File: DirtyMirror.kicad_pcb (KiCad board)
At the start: 2 copper layers, 53 parts, among them J101 PWR, SW101 SW_SPDT, U101 TL074, U102 TL074, U103 TL072

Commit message: routed & DRC passing
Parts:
- added C109: 4n7, Capacitor_SMD:C_0805_2012Metric, B.Cu at (21.7, 62.6)
- added C111: 2n2, Capacitor_SMD:C_0805_2012Metric, B.Cu at (14.1, 66.5)
- added J102: ScopeGroundLoop, Connector:THT_GND_WIRE, B.Cu at (84.7, 68.4)
- added TP101: In, TestPoint:TestPoint_THTPad_D2.0mm_Drill1.0mm_VAL, B.Cu at (36.4, 88.2)
- added TP102: Out, TestPoint:TestPoint_THTPad_D2.0mm_Drill1.0mm_VAL, B.Cu at (60.7, 86.5)
- added TP103: LT, TestPoint:TestPoint_THTPad_D2.0mm_Drill1.0mm_VAL, B.Cu at (30.9, 80.1)
- added TP104: HT, TestPoint:TestPoint_THTPad_D2.0mm_Drill1.0mm_VAL, B.Cu at (16.1, 82.2)
- added TP105: Bias, TestPoint:TestPoint_THTPad_D2.0mm_Drill1.0mm_VAL, B.Cu at (46.9, 67.2)
- added TP106: LR, TestPoint:TestPoint_THTPad_D2.0mm_Drill1.0mm_VAL, B.Cu at (64.2, 54.7)
- added TP107: HR, TestPoint:TestPoint_THTPad_D2.0mm_Drill1.0mm_VAL, B.Cu at (55.0, 58.1)
- added TP108: FF, TestPoint:TestPoint_THTPad_D2.0mm_Drill1.0mm_VAL, B.Cu at (28.6, 58.2)
- added TP109: GG, TestPoint:TestPoint_THTPad_D2.0mm_Drill1.0mm_VAL, B.Cu at (11.2, 69.6)
- C110, J101, SW101: moved to B.Cu
- R106, R107: value 47k -> 22k
- R123: value 100k -> 47k
- U101, U102: footprint Package_SO:SOIC-14_3.9x8.7mm_P1.27mm -> Package_DIP:DIP-14_W7.62mm
- U103: footprint Package_SO:SOIC-8_3.9x4.9mm_P1.27mm -> Package_DIP:DIP-8_W7.62mm
- moved C105 53.8 mm to (10.6, 65.7), turned to -90 degrees
- moved U103 52.4 mm to (10.6, 55.0), turned to -90 degrees
- moved R122 50.8 mm to (8.05, 51.0), turned to 180 degrees
- moved R123 44.3 mm to (17.8, 66.5), turned to 0 degrees
- moved C110 36.3 mm to (34.6, 53.1), turned to 180 degrees
- moved R121 35.6 mm to (28.6, 62.9), turned to 90 degrees
- moved R116 34.8 mm to (68.1, 77.0), turned to -90 degrees
- moved D104 31.4 mm to (67.6, 60.3), turned to 90 degrees
- moved R114 29.2 mm to (64.7, 65.7), turned to 180 degrees
- moved R117 28.7 mm to (64.8, 77.0), turned to -90 degrees
- moved D103 26.9 mm to (63.8, 60.4), turned to -90 degrees
- moved D102 21.8 mm to (47.2, 79.9), turned to 90 degrees
- moved R115 21.3 mm to (64.7, 69.0), turned to 180 degrees
- moved U101 19.4 mm to (38.5, 61.7)
- moved R129 18.8 mm to (51.2, 58.2), turned to 90 degrees
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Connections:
- R108 pad 2: /Gtr_Gain -> Net-(R108-Pad2)
- R109 pad 2: Net-(U101D--) -> Net-(U103A--)
- R111 pad 1: /Gtr_Gain -> /Gtr_gain
- R114 pad 1: /Gtr_Gain -> /Gtr_gain
- R120 pad 1: /Gtr_Gain -> /Gtr_gain
- R120 pad 2: Net-(U103A--) -> Net-(U101D--)
- R121 pad 1: Net-(U103A--) -> Net-(U101D--)
- R121 pad 2: Net-(R121-Pad2) -> /FxFull
- R122 pad 1: Net-(R121-Pad2) -> Net-(R108-Pad2)
- R122 pad 2: Net-(U103B--) -> Net-(C111-Pad1)
- R123 pad 1: Net-(U103B--) -> Net-(C111-Pad1)
- R123 pad 2: /FxFull -> Net-(U103B-+)
- RV102 pad 1: Net-(U101D--) -> Net-(U103A--)
- RV103 pad 1: Net-(U103A--) -> Net-(R118-Pad2)
- RV103 pad 2: Net-(U103A--) -> Net-(R118-Pad2)
- RV103 pad 3: Net-(R118-Pad2) -> Net-(U101D--)
- RV103 pad 4: Net-(U103A--) -> Net-(R119-Pad2)
- RV103 pad 5: Net-(U103A--) -> Net-(R119-Pad2)
- RV103 pad 6: Net-(R119-Pad2) -> Net-(U101D--)
- U101 pad 14: /Gtr_Gain -> /FxFull
- U103 pad 1: Net-(R121-Pad2) -> Net-(R108-Pad2)
- U103 pad 5: /Bias -> Net-(U103B-+)
- U103 pad 6: Net-(U103B--) -> /Gtr_gain
- U103 pad 7: /FxFull -> /Gtr_gain
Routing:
- net /Gtr_gain: track 0.00 -> 131.0 mm, vias 0 -> 4
- net +9V: track 0.00 -> 107.0 mm, vias 0 -> 1
- net /Bias: track 0.00 -> 80.0 mm, vias 0 -> 1
- net Net-(C103-Pad2): track 0.00 -> 68.0 mm, vias 0 -> 2
- net /FxFull: track 0.00 -> 67.4 mm
- net /LoThresh: track 0.00 -> 51.0 mm
- net /LoRect: track 0.00 -> 47.1 mm
- net /HiThresh: track 0.00 -> 47.0 mm
- net Net-(U101D--): track 0.00 -> 40.6 mm
- net Net-(D102-A): track 0.00 -> 37.3 mm
- net Net-(SW101-B): track 0.00 -> 34.4 mm
- net Net-(C111-Pad1): track 0.00 -> 33.8 mm
- net Net-(C106-Pad2): track 0.00 -> 20.5 mm
- net Net-(D104-K): track 0.00 -> 20.4 mm
- net FX_OUT: track 0.00 -> 19.1 mm
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- added copper zone on B.Cu, net GND
- added copper zone on F.Cu, net GND
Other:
- board outline added: 84 x 49 mm
- board text added: "+9V"
- board text added: "GND"
- board text added: "IN"
- board text added: "OUT"

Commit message: rev2 simulation
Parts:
- C103, C106: value 1u -> 2u2
- C111: value 2n2 -> 2n7
- R102: value 10k -> 22k
- R108, R109: value 3k3 -> 22k
- R121: value 47k -> 100k
- RV101: value 10k -> 10kB
- RV102: value 10kB -> 100kB
- moved J102 15.8 mm to (78.5, 83.0), turned to 0 degrees
- moved C102 2.75 mm to (41.0, 58.3)
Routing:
- net /Bias: track 80.0 -> 88.9 mm
- net Net-(U101A-+): track 10.7 -> 14.1 mm
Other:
- board size 84 x 49 mm -> 82 x 49 mm
- board text added: "Dirty Mirror"
- board text added: "Rev. 1- Dec. 2023 Hayden Setlik"

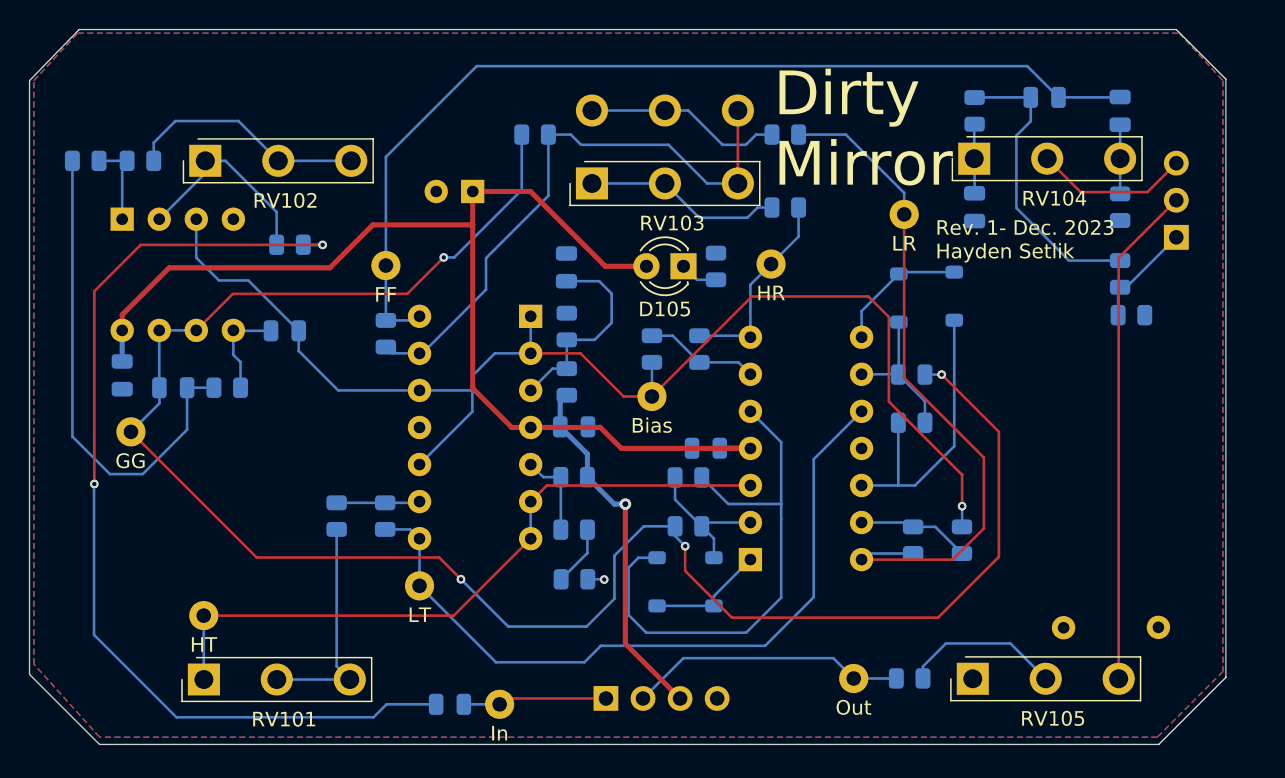
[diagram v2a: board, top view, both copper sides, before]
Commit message: rev2 passive vals dialed in
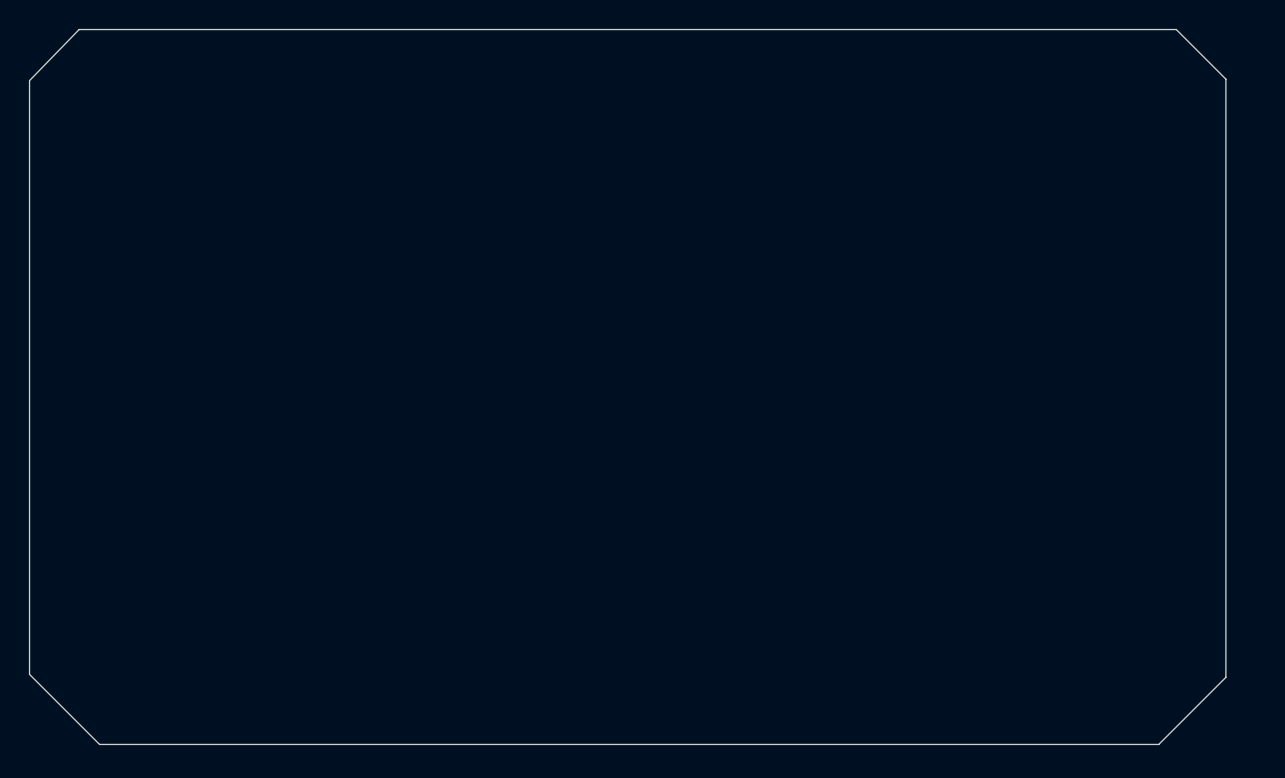
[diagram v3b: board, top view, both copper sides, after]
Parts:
- removed C101, C102, C104, C105, C107, C108: 100n, Capacitor_SMD:C_0805_2012Metric
- removed C103, C106: 2u2, Capacitor_SMD:C_0805_2012Metric
- removed C109: 4n7, Capacitor_SMD:C_0805_2012Metric
- removed C110: 100u, Capacitor_THT:CP_Radial_D5.0mm_P2.50mm
- removed C111: 2n7, Capacitor_SMD:C_0805_2012Metric
- removed D101, D102, D103, D104: 1N4148W, Diode_SMD:D_SOD-123
- removed D105: LED, LED_THT:LED_D3.0mm
- removed J101: PWR, Connector_PinHeader_2.54mm:PinHeader_1x04_P2.54mm_Vertical
- removed J102: ScopeGroundLoop, Connector:THT_GND_WIRE
- removed R101, R103, R104, R105, R110, R111, R112, R113, R114, R115, R116, R117, R121, R126, R127: 100k, Resistor_SMD:R_0805_2012Metric
- removed R102, R106, R107, R108, R109: 22k, Resistor_SMD:R_0805_2012Metric
- removed R118, R119, R120, R122, R123: 47k, Resistor_SMD:R_0805_2012Metric
- removed R124: 1k8, Resistor_SMD:R_0805_2012Metric
- removed R125: 5k6, Resistor_SMD:R_0805_2012Metric
- removed R128: 220R, Resistor_SMD:R_0805_2012Metric
- removed R129: 3k3, Resistor_SMD:R_0805_2012Metric
- removed RV101, RV104: 10kB, Potentiometer_THT:Potentiometer_Alpha_RV16AF_42_Single_Long
- removed RV102: 100kB, Potentiometer_THT:Potentiometer_Alpha_RV16AF_42_Single_Long
- removed RV103: 100kB, Potentiometer_THT:Potentiometer_Alpha_RV16A01F_41_Dual_Long
- removed RV105: 100kA, Potentiometer_THT:Potentiometer_Alpha_RV16AF_42_Single_Long
- removed SW101: SW_SPDT, Connector_PinSocket_2.54mm:PinSocket_1x03_P2.54mm_Vertical
- removed TP101: In, TestPoint:TestPoint_THTPad_D2.0mm_Drill1.0mm_VAL
- removed TP102: Out, TestPoint:TestPoint_THTPad_D2.0mm_Drill1.0mm_VAL
- removed TP103: LT, TestPoint:TestPoint_THTPad_D2.0mm_Drill1.0mm_VAL
- removed TP104: HT, TestPoint:TestPoint_THTPad_D2.0mm_Drill1.0mm_VAL
- removed TP105: Bias, TestPoint:TestPoint_THTPad_D2.0mm_Drill1.0mm_VAL
- removed TP106: LR, TestPoint:TestPoint_THTPad_D2.0mm_Drill1.0mm_VAL
- removed TP107: HR, TestPoint:TestPoint_THTPad_D2.0mm_Drill1.0mm_VAL
- removed TP108: FF, TestPoint:TestPoint_THTPad_D2.0mm_Drill1.0mm_VAL
- removed TP109: GG, TestPoint:TestPoint_THTPad_D2.0mm_Drill1.0mm_VAL
- removed U101, U102: TL074, Package_DIP:DIP-14_W7.62mm
- removed U103: TL072, Package_DIP:DIP-8_W7.62mm
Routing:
- net /Gtr_gain: track 131.0 -> 0.00 mm, vias 4 -> 0
- net +9V: track 107.0 -> 0.00 mm, vias 1 -> 0
- net /Bias: track 88.9 -> 0.00 mm, vias 1 -> 0
- net Net-(C103-Pad2): track 68.0 -> 0.00 mm, vias 2 -> 0
- net /FxFull: track 67.4 -> 0.00 mm
- net /LoThresh: track 51.0 -> 0.00 mm
- net /LoRect: track 47.1 -> 0.00 mm
- net /HiThresh: track 47.0 -> 0.00 mm
- net Net-(U101D--): track 40.6 -> 0.00 mm
- net Net-(D102-A): track 37.3 -> 0.00 mm
- net Net-(SW101-B): track 34.4 -> 0.00 mm
- net Net-(C111-Pad1): track 33.8 -> 0.00 mm
- net Net-(C106-Pad2): track 20.5 -> 0.00 mm
- net Net-(D104-K): track 20.4 -> 0.00 mm
- net FX_OUT: track 19.1 -> 0.00 mm
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- removed copper zone on B.Cu, net GND
- removed copper zone on F.Cu, net GND
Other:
- board text removed: "+9V"
- board text removed: "Dirty Mirror"
- board text removed: "GND"
- board text removed: "IN"
- board text removed: "OUT"
- board text removed: "Rev. 1- Dec. 2023 Hayden Setlik"

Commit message: rev2 rough routing
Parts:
- added C101: 100n, Capacitor_SMD:C_0805_2012Metric, B.Cu at (41.6, 62.0)
- added C102: 100n, Capacitor_SMD:C_0805_2012Metric, B.Cu at (45.5, 69.0)
- added C103: 2u2, Capacitor_SMD:C_0805_2012Metric, B.Cu at (21.8, 54.6)
- added C104: 100n, Capacitor_SMD:C_0805_2012Metric, B.Cu at (52.4, 68.5)
- added C106: 2u2, Capacitor_SMD:C_0805_2012Metric, B.Cu at (73.6, 46.5)
- added C107: 100n, Capacitor_SMD:C_0805_2012Metric, B.Cu at (79.0, 47.4)
- added C108: 100n, Capacitor_SMD:C_0805_2012Metric, B.Cu at (69.0, 54.3)
- added C109: 4n7, Capacitor_SMD:C_0805_2012Metric, B.Cu at (27.2, 59.5)
- added C110: 100u, Capacitor_THT:CP_Radial_D5.0mm_P2.50mm, B.Cu at (47.9, 63.4)
- added C111: 2n7, Capacitor_SMD:C_0805_2012Metric, B.Cu at (27.6, 69.6)
- added D101: 1N4148W, Diode_SMD:D_SOD-123, B.Cu at (52.1, 79.7)
- added D102: 1N4148W, Diode_SMD:D_SOD-123, B.Cu at (48.1, 79.7)
- added D103: 1N4148W, Diode_SMD:D_SOD-123, B.Cu at (67.3, 61.5)
- added D104: 1N4148W, Diode_SMD:D_SOD-123, B.Cu at (71.2, 61.5)
- added D105: LED, LED_THT:LED_D3.0mm, F.Cu at (49.0, 58.2)
- added J101: PWR, Connector_PinHeader_2.54mm:PinHeader_1x04_P2.54mm_Vertical, B.Cu at (44.0, 88.3)
- added J102: ScopeGroundLoop, Connector:THT_GND_WIRE, B.Cu at (11.4, 60.8)
- added R101: 56k, Resistor_SMD:R_0805_2012Metric, B.Cu at (53.0, 71.4)
- added R102: 1k, Resistor_SMD:R_0805_2012Metric, B.Cu at (16.2, 54.6)
- added R103: 68k, Resistor_SMD:R_0805_2012Metric, B.Cu at (49.6, 71.4)
- added R104: 100k, Resistor_SMD:R_0805_2012Metric, B.Cu at (42.1, 64.8)
- added R105: 100k, Resistor_SMD:R_0805_2012Metric, B.Cu at (42.1, 68.6)
- added R106: 56k, Resistor_SMD:R_0805_2012Metric, B.Cu at (16.1, 82.9)
- added R107: 68k, Resistor_SMD:R_0805_2012Metric, B.Cu at (26.2, 82.9)
- added R108: 680k, Resistor_SMD:R_0805_2012Metric, B.Cu at (27.4, 54.6)
- added R109: 100k, Resistor_SMD:R_0805_2012Metric, B.Cu at (25.2, 54.6)
- added R110: 100k, Resistor_SMD:R_0805_2012Metric, B.Cu at (51.9, 75.4)
- added R111: 100k, Resistor_SMD:R_0805_2012Metric, B.Cu at (49.2, 75.4)
- added R112: 100k, Resistor_SMD:R_0805_2012Metric, B.Cu at (56.9, 59.0)
- added R113: 100k, Resistor_SMD:R_0805_2012Metric, B.Cu at (60.4, 59.0)
- added R114: 100k, Resistor_SMD:R_0805_2012Metric, B.Cu at (66.1, 66.3)
- added R115: 100k, Resistor_SMD:R_0805_2012Metric, B.Cu at (69.5, 66.3)
- added R116: 100k, Resistor_SMD:R_0805_2012Metric, B.Cu at (63.6, 59.0)
- added R117: 100k, Resistor_SMD:R_0805_2012Metric, B.Cu at (53.1, 64.3)
- added R118: 47k, Resistor_SMD:R_0805_2012Metric, B.Cu at (55.7, 83.1)
- added R119: 68k, Resistor_SMD:R_0805_2012Metric, B.Cu at (59.1, 83.1)
- added R120: 47k, Resistor_SMD:R_0805_2012Metric, B.Cu at (62.5, 83.1)
- added R121: 68k, Resistor_SMD:R_0805_2012Metric, B.Cu at (65.2, 77.0)
- added R122: 47k, Resistor_SMD:R_0805_2012Metric, B.Cu at (23.1, 65.6)
- added R123: 47k, Resistor_SMD:R_0805_2012Metric, B.Cu at (27.6, 62.9)
- added R124: 1k8, Resistor_SMD:R_0805_2012Metric, B.Cu at (79.0, 54.3)
- added R125: 5k6, Resistor_SMD:R_0805_2012Metric, B.Cu at (69.0, 47.4)
- added R126: 100k, Resistor_SMD:R_0805_2012Metric, B.Cu at (79.2, 62.9)
- added R127: 100k, Resistor_SMD:R_0805_2012Metric, B.Cu at (75.9, 62.9)
- added R128: 220R, Resistor_SMD:R_0805_2012Metric, B.Cu at (72.9, 83.8)
- added R129: 4k7, Resistor_SMD:R_0805_2012Metric, B.Cu at (52.1, 58.1)
- added R130: 33k, Resistor_SMD:R_0805_2012Metric, B.Cu at (27.6, 66.2)
- added R131: 10k, Resistor_SMD:R_0805_2012Metric, B.Cu at (34.5, 72.6)
- added R132: 4k7, Resistor_SMD:R_0805_2012Metric, B.Cu at (52.8, 47.2)
- added R133: 47k, Resistor_SMD:R_0805_2012Metric, B.Cu at (52.8, 54.4)
- added R134: 4k7, Resistor_SMD:R_0805_2012Metric, B.Cu at (42.8, 47.2)
- added R135: 47k, Resistor_SMD:R_0805_2012Metric, B.Cu at (46.1, 54.1)
- added R136: 100k, Resistor_SMD:R_0805_2012Metric, B.Cu at (40.9, 55.6)
- added RV101: 10kB, Potentiometer_THT:Potentiometer_Alpha_RV16AF_42_Single_Long, F.Cu at (16.1, 86.5)
- added RV102: 10k, Potentiometer_THT:Potentiometer_Alpha_RV16AF_42_Single_Long, F.Cu at (16.2, 51.0)
- added RV103: 10kB, Potentiometer_THT:Potentiometer_Alpha_RV16AF_42_Single_Long, F.Cu at (42.8, 50.9)
- added RV104: 10kB, Potentiometer_THT:Potentiometer_Alpha_RV16AF_42_Single_Long, F.Cu at (69.0, 50.9)
- added RV105: 100kA, Potentiometer_THT:Potentiometer_Alpha_RV16AF_42_Single_Long, F.Cu at (68.8, 86.5)
- added SW101: SW_SPDT, Connector_PinSocket_2.54mm:PinSocket_1x03_P2.54mm_Vertical, B.Cu at (82.5, 63.4)
- added TP101: In, TestPoint:TestPoint_THTPad_D2.0mm_Drill1.0mm_VAL, B.Cu at (21.8, 59.1)
- added TP102: Out, TestPoint:TestPoint_THTPad_D2.0mm_Drill1.0mm_VAL, B.Cu at (69.2, 83.4)
- added TP103: LT, TestPoint:TestPoint_THTPad_D2.0mm_Drill1.0mm_VAL, B.Cu at (39.6, 83.8)
- added TP104: HT, TestPoint:TestPoint_THTPad_D2.0mm_Drill1.0mm_VAL, B.Cu at (45.7, 72.3)
- added TP105: Bias, TestPoint:TestPoint_THTPad_D2.0mm_Drill1.0mm_VAL, B.Cu at (38.6, 72.5)
- added TP106: LR, TestPoint:TestPoint_THTPad_D2.0mm_Drill1.0mm_VAL, B.Cu at (63.6, 54.5)
- added TP107: HR, TestPoint:TestPoint_THTPad_D2.0mm_Drill1.0mm_VAL, B.Cu at (44.0, 79.8)
- added TP108: FF, TestPoint:TestPoint_THTPad_D2.0mm_Drill1.0mm_VAL, B.Cu at (38.6, 50.0)
- added TP109: GG, TestPoint:TestPoint_THTPad_D2.0mm_Drill1.0mm_VAL, B.Cu at (31.0, 72.8)
- added TP110: CLIP, TestPoint:TestPoint_THTPad_D2.0mm_Drill1.0mm_VAL, B.Cu at (55.7, 46.3)
- added TP111: FOLD, TestPoint:TestPoint_THTPad_D2.0mm_Drill1.0mm_VAL, B.Cu at (45.6, 46.3)
- added U101: TL074, Package_DIP:DIP-14_W7.62mm, B.Cu at (38.6, 54.3)
- added U102: TL074, Package_DIP:DIP-14_W7.62mm, B.Cu at (55.4, 78.2)
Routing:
- net /Gtr_gain: track 0.00 -> 96.8 mm, vias 0 -> 4
- net /Bias: track 0.00 -> 96.8 mm
- net +9V: track 0.00 -> 91.4 mm, vias 0 -> 1
- net /HiRect: track 0.00 -> 80.0 mm, vias 0 -> 2
- net /FxFull: track 0.00 -> 58.6 mm
- net /LoThresh: track 0.00 -> 54.3 mm, vias 0 -> 1
- net /Fold: track 0.00 -> 51.4 mm
- net FX_IN: track 0.00 -> 47.8 mm
- net /LoRect: track 0.00 -> 44.0 mm
- net Net-(R122-Pad1): track 0.00 -> 31.0 mm
- net Net-(SW101-B): track 0.00 -> 28.9 mm
- net FX_OUT: track 0.00 -> 27.6 mm
- net Net-(C106-Pad2): track 0.00 -> 23.0 mm
- net /Clip: track 0.00 -> 22.2 mm
- net Net-(U102D--): track 0.00 -> 18.4 mm
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- added copper zone on B.Cu, net GND
- added copper zone on F.Cu, net GND

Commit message: silkscreen, DRC passing
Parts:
- added REF**: IN, Symbol:VAL_LABEL_1.5mm_DOUBLE, F.Cu at (45.3, 86.6)
- added REF**: OUT, Symbol:VAL_LABEL_1.5mm_DOUBLE, F.Cu at (47.8, 86.5)
- added REF**: +9V, Symbol:VAL_LABEL_1.5mm_DOUBLE, F.Cu at (50.5, 86.6)
- added REF**: GND, Symbol:VAL_LABEL_1.5mm_DOUBLE, F.Cu at (53.1, 86.6)
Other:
- board text added: "Dirty Mirror"
- board text added: "Rev 2- Jan 2025 Hayden Setlik"

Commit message: pedal working, tweaked a few component values
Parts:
- C109: value 4n7 -> 10n
- R102: value 1k -> 2k2
- R106: value 56k -> 68k
- R107: value 68k -> 56k
- R108: value 680k -> 820k
- R109: value 100k -> 180k
- R118, R120, R122, R123: value 47k -> 33k
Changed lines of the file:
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@@
 			)
 		)
-		(property "Value" "56k"
+		(property "Value" "68k"
 			(at 0 -1.65 90)
 			(layer "B.Fab")
@@
 			)
 		)
-		(property "Value" "47k"
+		(property "Value" "33k"
 			(at 0 -1.65 90)
 			(layer "B.Fab")
@@
 			)
 		)
-		(property "Value" "47k"
+		(property "Value" "33k"
 			(at 0 -1.65 90)
 			(layer "B.Fab")
@@
 			)
 		)
-		(property "Value" "100k"
+		(property "Value" "180k"
 			(at 0 -1.65 90)
 			(layer "B.Fab")
@@
 			)
 		)
-		(property "Value" "1k"
+		(property "Value" "2k2"
 			(at 0 -1.65 90)
 			(layer "B.Fab")
@@
 			)
 		)
-		(property "Value" "47k"
+		(property "Value" "33k"
 			(at 0 -1.65 90)
 			(layer "B.Fab")
@@
 			)
 		)
-		(property "Value" "68k"
+		(property "Value" "56k"
 			(at 0 -1.65 90)
 			(layer "B.Fab")
@@
 			)
 		)
-		(property "Value" "4n7"
+		(property "Value" "10n"
 			(at 0 -1.679999 90)
 			(layer "B.Fab")
@@
 			)
 		)
-		(property "Value" "47k"
+		(property "Value" "33k"
 			(at 0 -1.65 0)
 			(layer "B.Fab")
@@
 			)
 		)
-		(property "Value" "680k"
+		(property "Value" "820k"
 			(at 0 -1.65 90)
 			(layer "B.Fab")

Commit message: threshold/summing amp value tweaks
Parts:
- R108: value 820k -> 560k
- R109: value 180k -> 100k
- R112, R117: value 100k -> 5k1
- R113, R116: value 100k -> 5k6
- R118, R120: value 33k -> 4k7
- R119, R121: value 68k -> 5k6
- R136: value 100k -> 180k
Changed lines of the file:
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@@
 			)
 		)
-		(property "Value" "100k"
+		(property "Value" "5k1"
 			(at 0 -1.65 90)
 			(layer "B.Fab")
@@
 			)
 		)
-		(property "Value" "100k"
+		(property "Value" "180k"
 			(at 0 -1.65 90)
 			(layer "B.Fab")
@@
 			)
 		)
-		(property "Value" "100k"
+		(property "Value" "5k6"
 			(at 0 -1.65 90)
 			(layer "B.Fab")
@@
 			)
 		)
-		(property "Value" "68k"
+		(property "Value" "5k6"
 			(at 0 -1.65 90)
 			(layer "B.Fab")
@@
 			)
 		)
-		(property "Value" "68k"
+		(property "Value" "5k6"
 			(at 0 -1.65 90)
 			(layer "B.Fab")
@@
 			)
 		)
-		(property "Value" "33k"
+		(property "Value" "4k7"
 			(at 0 -1.65 90)
 			(layer "B.Fab")
@@
 			)
 		)
-		(property "Value" "180k"
+		(property "Value" "100k"
 			(at 0 -1.65 90)
 			(layer "B.Fab")
@@
 			)
 		)
-		(property "Value" "100k"
+		(property "Value" "5k1"
 			(at 0 -1.65 90)
 			(layer "B.Fab")
@@
 			)
 		)
-		(property "Value" "33k"
+		(property "Value" "4k7"
 			(at 0 -1.65 90)
 			(layer "B.Fab")
@@
 			)
 		)
-		(property "Value" "100k"
+		(property "Value" "5k6"
 			(at 0 -1.65 90)
 			(layer "B.Fab")
@@
 			)
 		)
-		(property "Value" "820k"
+		(property "Value" "560k"
 			(at 0 -1.65 90)
 			(layer "B.Fab")

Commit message: optimized rev2 component values :)
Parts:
- R101, R107: value 56k -> 47k
- R103, R106: value 68k -> 51k
- R112, R117: value 5k1 -> 51k
- R113, R116, R119, R121: value 5k6 -> 56k
- R118, R120: value 4k7 -> 47k
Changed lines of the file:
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@@
 			)
 		)
-		(property "Value" "68k"
+		(property "Value" "51k"
 			(at 0 -1.65 90)
 			(layer "B.Fab")
@@
 			)
 		)
-		(property "Value" "5k1"
+		(property "Value" "51k"
 			(at 0 -1.65 90)
 			(layer "B.Fab")
@@
 			)
 		)
-		(property "Value" "68k"
+		(property "Value" "51k"
 			(at 0 -1.65 90)
 			(layer "B.Fab")
@@
 			)
 		)
-		(property "Value" "56k"
+		(property "Value" "47k"
 			(at 0 -1.65 90)
 			(layer "B.Fab")
@@
 			)
 		)
-		(property "Value" "5k6"
+		(property "Value" "56k"
 			(at 0 -1.65 90)
 			(layer "B.Fab")
@@
 			)
 		)
-		(property "Value" "5k6"
+		(property "Value" "56k"
 			(at 0 -1.65 90)
 			(layer "B.Fab")
@@
 			)
 		)
-		(property "Value" "5k6"
+		(property "Value" "56k"
 			(at 0 -1.65 90)
 			(layer "B.Fab")
@@
 			)
 		)
-		(property "Value" "4k7"
+		(property "Value" "47k"
 			(at 0 -1.65 90)
 			(layer "B.Fab")
@@
 			)
 		)
-		(property "Value" "5k1"
+		(property "Value" "51k"
 			(at 0 -1.65 90)
 			(layer "B.Fab")
@@
 			)
 		)
-		(property "Value" "4k7"
+		(property "Value" "47k"
 			(at 0 -1.65 90)
 			(layer "B.Fab")
@@
 			)
 		)
-		(property "Value" "56k"
+		(property "Value" "47k"
 			(at 0 -1.65 90)
 			(layer "B.Fab")
@@
 			)
 		)
-		(property "Value" "5k6"
+		(property "Value" "56k"
 			(at 0 -1.65 90)
 			(layer "B.Fab")
